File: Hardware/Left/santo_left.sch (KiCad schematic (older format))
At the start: 7 parts

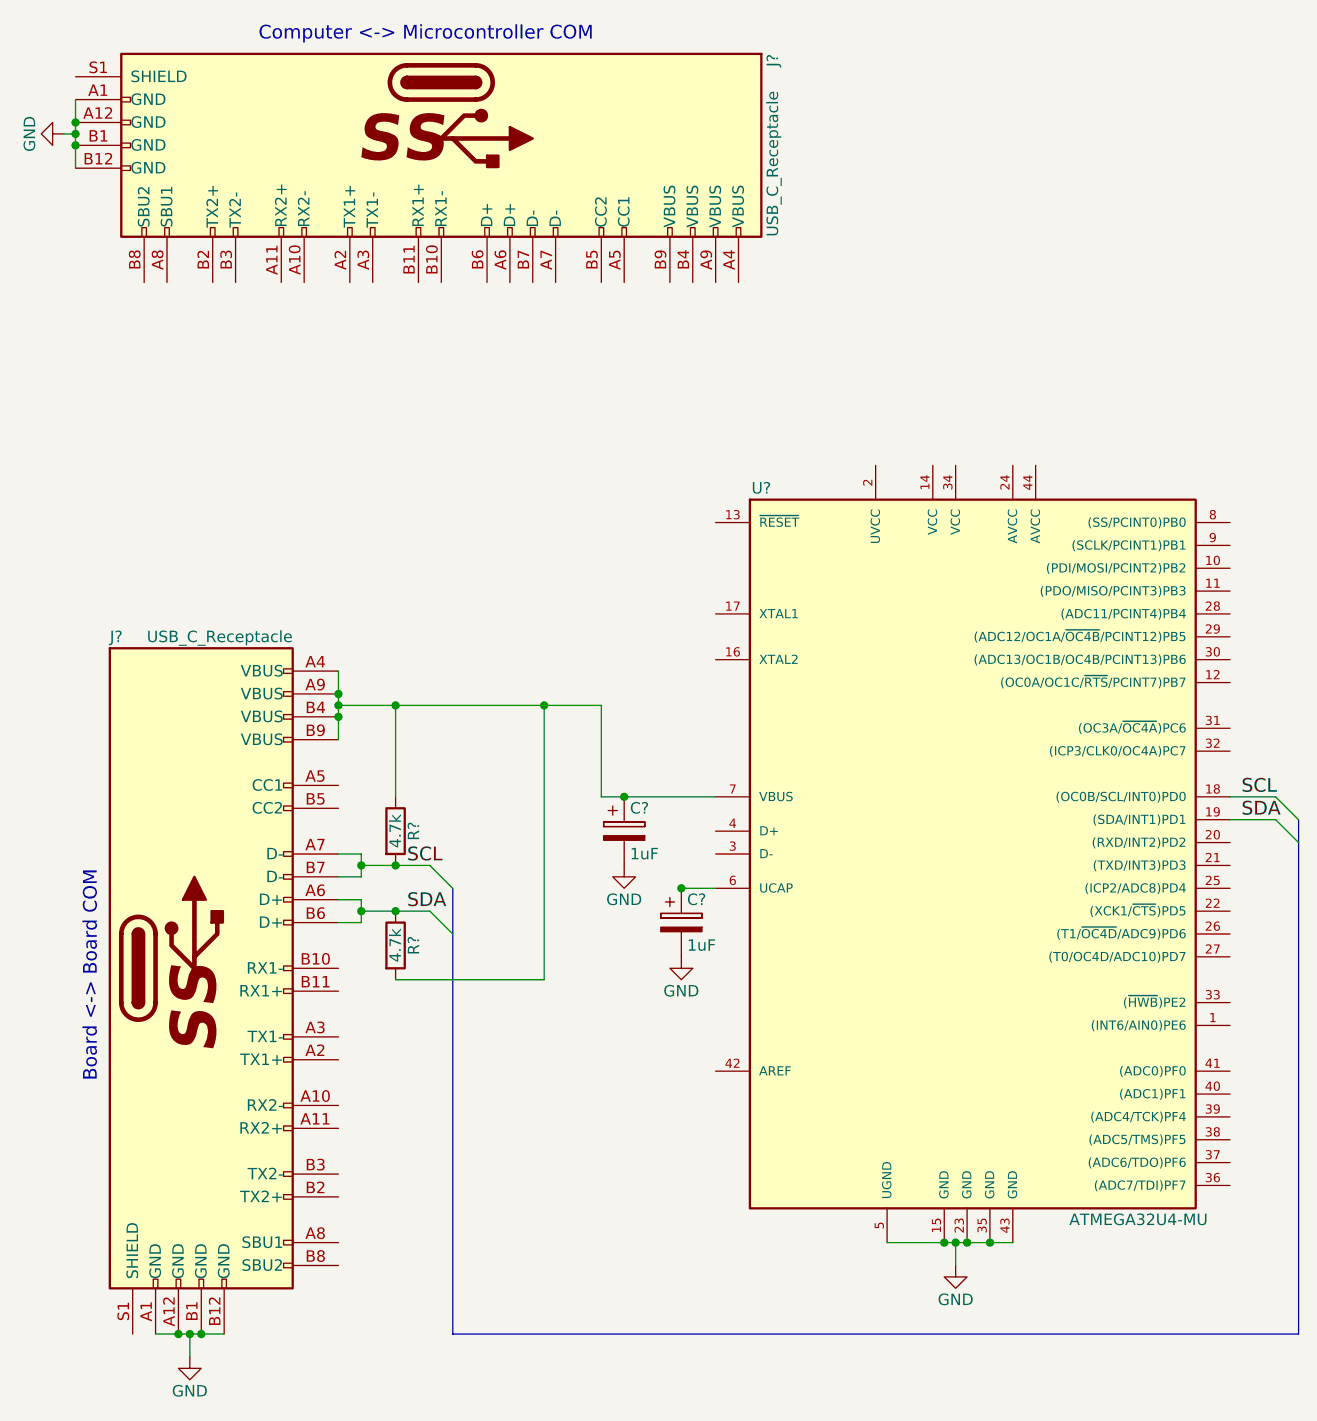
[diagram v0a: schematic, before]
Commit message: Wire up the PC <-> Board communication.
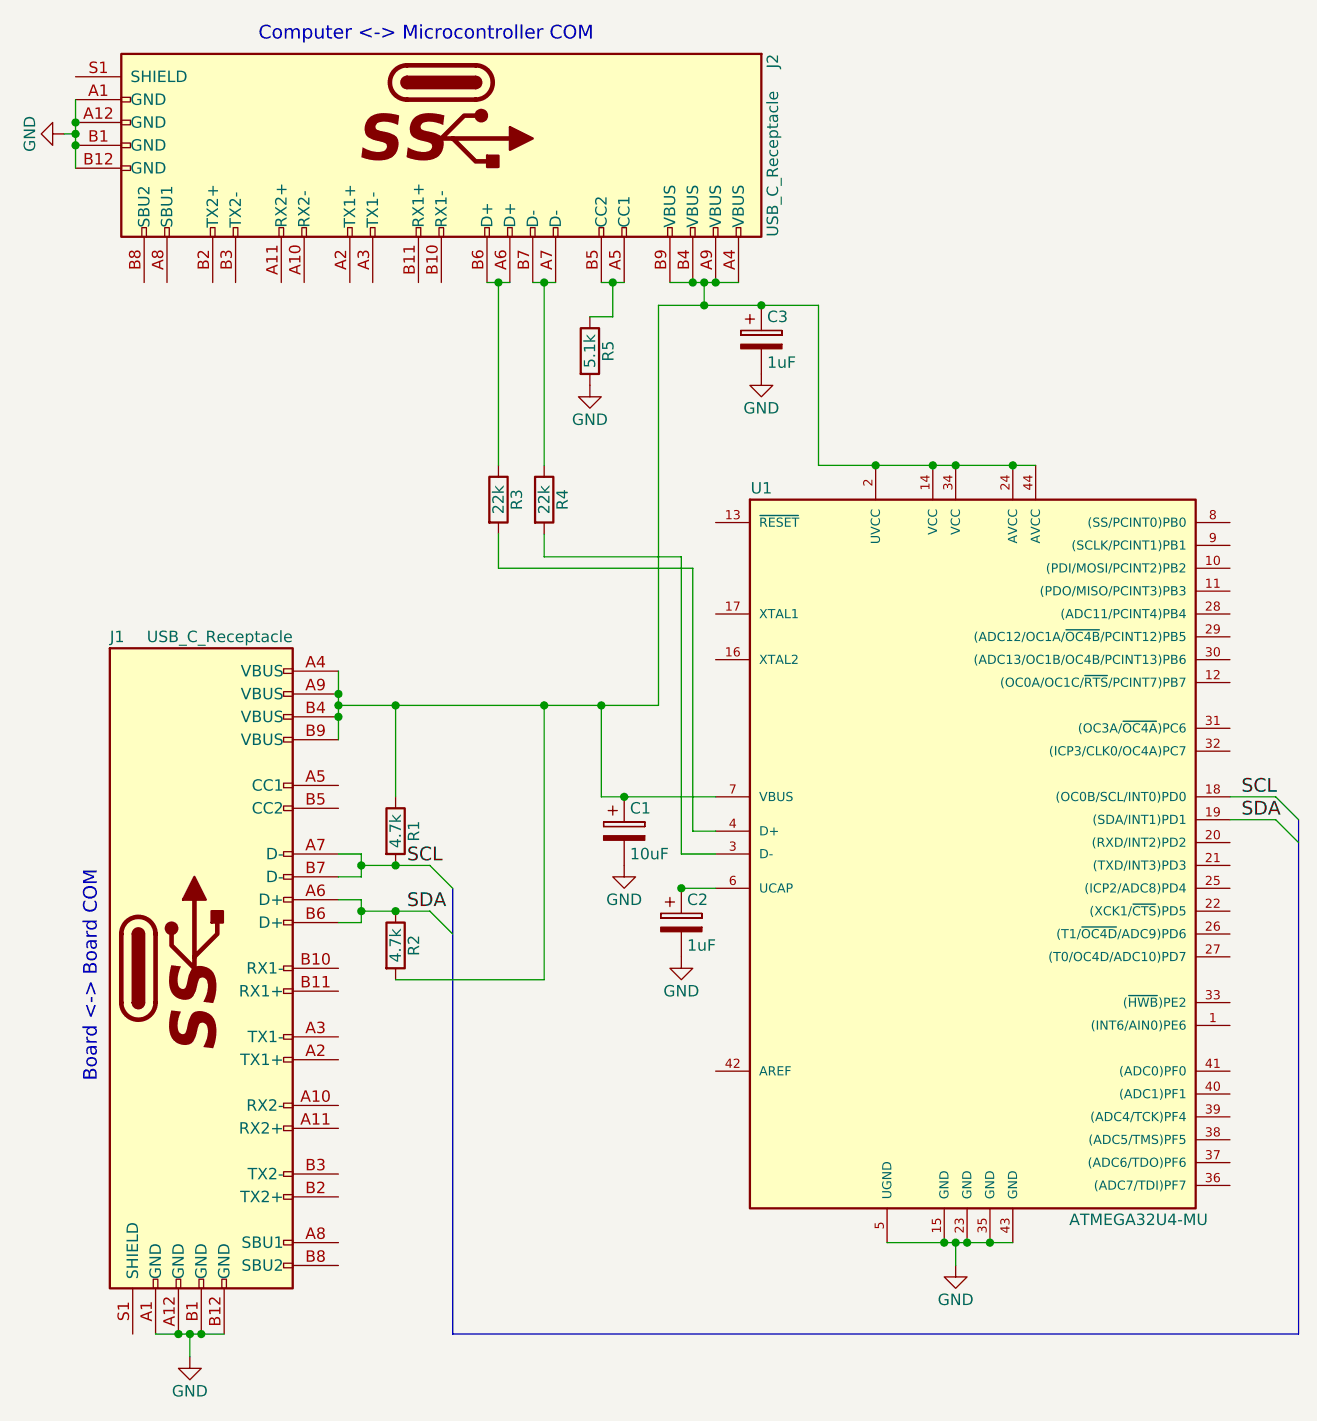
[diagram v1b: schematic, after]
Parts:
- added C3: 1uF, symbol CP
- added R3, R4: 22k, symbol R
- added R5: 5.1k, symbol R
- C1: renamed from C?; value 1uF -> 10uF
- gave numbers to parts that had none: 6
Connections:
- net GND: now also C3.2, R5.2
- net at U1.14 (VCC): now also C1.1, J1.A4 (VBUS), J1.A9 (VBUS), J1.B4 (VBUS), J1.B9 (VBUS), J2.A4 (VBUS), J2.A9 (VBUS), J2.B4 (VBUS), J2.B9 (VBUS), R1.1, R2.2, U1.2 (UVCC), U1.24 (AVCC), U1.34 (VCC), U1.44 (AVCC), U1.7 (VBUS), C3.1
- net at U1.3 (D-): now also R4.2
- net at U1.4 (D+): now also R3.2
- net at J2.A5 (CC1): now also J2.B5 (CC2), R5.1
- net at J2.A6 (D+): now also J2.B6 (D+), R3.1
- net at J2.A7 (D-): now also J2.B7 (D-), R4.1
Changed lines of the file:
@@
 $EndDescr
 $Comp
-L ATMEGA32U4-MU U?
+L ATMEGA32U4-MU U1
 U 1 1 5A091DA6
 P 4700 4300
-F 0 "U?" H 3750 6000 50  0000 C CNN
+F 0 "U1" H 3750 6000 50  0000 C CNN
 F 1 "ATMEGA32U4-MU" H 5400 2800 50  0000 C CNN
 F 2 "QFN44" H 4700 4300 50  0001 C CIN
@@
 $EndComp
 $Comp
-L USB_C_Receptacle J?
+L USB_C_Receptacle J2
 U 1 1 5A091DCC
 P 2350 1100
-F 0 "J?" H 1950 2550 50  0000 L CNN
+F 0 "J2" H 1950 2550 50  0000 L CNN
 F 1 "USB_C_Receptacle" H 2750 2550 50  0000 R CNN
 F 2 "" H 2500 1100 50  0001 C CNN
@@
 $EndComp
 $Comp
-L USB_C_Receptacle J?
+L USB_C_Receptacle J1
 U 1 1 5A091E31
 P 1300 4700
-F 0 "J?" H 900 6150 50  0000 L CNN
+F 0 "J1" H 900 6150 50  0000 L CNN
 F 1 "USB_C_Receptacle" H 1700 6150 50  0000 R CNN
 F 2 "" H 1450 4700 50  0001 C CNN
@@
 Entry Wire Line
 	6000 4050 6100 4150
-Wire Wire Line
-	5800 3950 6000 3950
-Wire Wire Line
-	5800 4050 6000 4050
-Wire Bus Line
-	6100 6300 6100 4050
-Wire Wire Line
-	1900 4200 2000 4200
-Wire Wire Line
-	2000 4300 1900 4300
-Wire Wire Line
-	1900 4400 2000 4400
-Wire Wire Line
-	1900 4500 2000 4500
-Wire Wire Line
-	2000 4200 2000 4300
-Wire Wire Line
-	2000 4500 2000 4400
-Connection ~ 2000 4250
-Connection ~ 2000 4450
-Wire Wire Line
-	3050 3950 3550 3950
-Wire Wire Line
-	1100 6300 1400 6300
-Wire Wire Line
-	1250 6300 1250 6400
-Connection ~ 1250 6300
-$Comp
-L GND #PWR?
+$Comp
+L GND #PWR2
 U 1 1 5A09277D
 P 1250 6400
-F 0 "#PWR?" H 1250 6150 50  0001 C CNN
+F 0 "#PWR2" H 1250 6150 50  0001 C CNN
 F 1 "GND" H 1250 6250 50  0000 C CNN
 F 2 "" H 1250 6400 50  0001 C CNN
@@
 	1    0    0    -1
 $EndComp
-Wire Wire Line
-	750  900  750  1200
-Wire Wire Line
-	750  1050 700  1050
-Connection ~ 750  1050
-$Comp
-L GND #PWR?
+$Comp
+L GND #PWR1
 U 1 1 5A0928F2
 P 700 1050
-F 0 "#PWR?" H 700 800 50  0001 C CNN
+F 0 "#PWR1" H 700 800 50  0001 C CNN
 F 1 "GND" H 700 900 50  0000 C CNN
 F 2 "" H 700 1050 50  0001 C CNN
@@
 	0    1    1    0
 $EndComp
-Wire Wire Line
-	3550 4350 3400 4350
-$Comp
-L CP C?
+$Comp
+L CP C2
 U 1 1 5A092A38
 P 3400 4500
-F 0 "C?" H 3425 4600 50  0000 L CNN
+F 0 "C2" H 3425 4600 50  0000 L CNN
 F 1 "1uF" H 3425 4400 50  0000 L CNN
 F 2 "" H 3438 4350 50  0001 C CNN
@@
 $EndComp
 $Comp
-L GND #PWR?
+L GND #PWR5
 U 1 1 5A092A79
 P 3400 4650
-F 0 "#PWR?" H 3400 4400 50  0001 C CNN
+F 0 "#PWR5" H 3400 4400 50  0001 C CNN
 F 1 "GND" H 3400 4500 50  0000 C CNN
 F 2 "" H 3400 4650 50  0001 C CNN
@@
 	1    0    0    -1
 $EndComp
+$Comp
+L CP C1
+U 1 1 5A0933EF
+P 3150 4100
+F 0 "C1" H 3175 4200 50  0000 L CNN
+F 1 "10uF" H 3175 4000 50  0000 L CNN
+F 2 "" H 3188 3950 50  0001 C CNN
+F 3 "" H 3150 4100 50  0001 C CNN
+	1    3150 4100
+	1    0    0    -1
+$EndComp
+$Comp
+L GND #PWR4
+U 1 1 5A09341E
+P 3150 4250
+F 0 "#PWR4" H 3150 4000 50  0001 C CNN
+F 1 "GND" H 3150 4100 50  0000 C CNN
+F 2 "" H 3150 4250 50  0001 C CNN
+F 3 "" H 3150 4250 50  0001 C CNN
+	1    3150 4250
+	1    0    0    -1
+$EndComp
+$Comp
+L GND #PWR7
+U 1 1 5A093698
+P 4600 6000
+F 0 "#PWR7" H 4600 5750 50  0001 C CNN
+F 1 "GND" H 4600 5850 50  0000 C CNN
+F 2 "" H 4600 6000 50  0001 C CNN
+F 3 "" H 4600 6000 50  0001 C CNN
+	1    4600 6000
+	1    0    0    -1
+$EndComp
+Text Label 5850 3950 0    60   ~ 0
+SCL
+Text Label 5850 4050 0    60   ~ 0
+SDA
+$Comp
+L R R1
+U 1 1 5A093ADE
+P 2150 4100
+F 0 "R1" V 2230 4100 50  0000 C CNN
+F 1 "4.7k" V 2150 4100 50  0000 C CNN
+F 2 "" V 2080 4100 50  0001 C CNN
+F 3 "" H 2150 4100 50  0001 C CNN
+	1    2150 4100
+	1    0    0    -1
+$EndComp
+$Comp
+L R R2
+U 1 1 5A093B19
+P 2150 4600
+F 0 "R2" V 2230 4600 50  0000 C CNN
+F 1 "4.7k" V 2150 4600 50  0000 C CNN
+F 2 "" V 2080 4600 50  0001 C CNN
+F 3 "" H 2150 4600 50  0001 C CNN
+	1    2150 4600
+	1    0    0    -1
+$EndComp
+Entry Wire Line
+	2300 4250 2400 4350
+Entry Wire Line
+	2300 4450 2400 4550
+Text Label 2200 4250 0    60   ~ 0
+SCL
+Text Label 2200 4450 0    60   ~ 0
+SDA
+$Comp
+L CP C3
+U 1 1 5A094C59
+P 3750 1950
+F 0 "C3" H 3775 2050 50  0000 L CNN
+F 1 "1uF" H 3775 1850 50  0000 L CNN
+F 2 "" H 3788 1800 50  0001 C CNN
+F 3 "" H 3750 1950 50  0001 C CNN
+	1    3750 1950
+	1    0    0    -1
+$EndComp
+$Comp
+L GND #PWR6
+U 1 1 5A094E64
+P 3750 2100
+F 0 "#PWR6" H 3750 1850 50  0001 C CNN
+F 1 "GND" H 3750 1950 50  0000 C CNN
+F 2 "" H 3750 2100 50  0001 C CNN
+F 3 "" H 3750 2100 50  0001 C CNN
+	1    3750 2100
+	1    0    0    -1
+$EndComp
+$Comp
+L R R5
+U 1 1 5A095F9F
+P 3000 2000
+F 0 "R5" V 3080 2000 50  0000 C CNN
+F 1 "5.1k" V 3000 2000 50  0000 C CNN
+F 2 "" V 2930 2000 50  0001 C CNN
+F 3 "" H 3000 2000 50  0001 C CNN
+	1    3000 2000
+	1    0    0    -1
+$EndComp
+$Comp
+L GND #PWR3
+U 1 1 5A095FF2
+P 3000 2150
+F 0 "#PWR3" H 3000 1900 50  0001 C CNN
+F 1 "GND" H 3000 2000 50  0000 C CNN
+F 2 "" H 3000 2150 50  0001 C CNN
+F 3 "" H 3000 2150 50  0001 C CNN
+	1    3000 2150
+	1    0    0    -1
+$EndComp
+Wire Wire Line
+	5800 3950 6000 3950
+Wire Wire Line
+	5800 4050 6000 4050
+Wire Bus Line
+	6100 6300 6100 4050
+Wire Wire Line
+	1900 4200 2000 4200
+Wire Wire Line
+	2000 4300 1900 4300
+Wire Wire Line
+	1900 4400 2000 4400
+Wire Wire Line
+	1900 4500 2000 4500
+Wire Wire Line
+	2000 4200 2000 4300
+Wire Wire Line
+	2000 4500 2000 4400
+Connection ~ 2000 4250
+Connection ~ 2000 4450
+Wire Wire Line
+	3050 3950 3550 3950
+Wire Wire Line
+	1100 6300 1400 6300
+Wire Wire Line
+	1250 6300 1250 6400
+Connection ~ 1250 6300
+Wire Wire Line
+	750  900  750  1200
+Wire Wire Line
+	750  1050 700  1050
+Connection ~ 750  1050
+Wire Wire Line
+	3550 4350 3400 4350
 Wire Wire Line
 	3050 3950 3050 3550
 Wire Wire Line
-	3050 3550 1900 3550
+	1900 3550 3300 3550
 Wire Wire Line
 	1900 3400 1900 3700
@@
 Connection ~ 750  1000
 Connection ~ 750  1100
-$Comp
-L CP C?
-U 1 1 5A0933EF
-P 3150 4100
-F 0 "C?" H 3175 4200 50  0000 L CNN
-F 1 "1uF" H 3175 4000 50  0000 L CNN
-F 2 "" H 3188 3950 50  0001 C CNN
-F 3 "" H 3150 4100 50  0001 C CNN
-	1    3150 4100
-	1    0    0    -1
-$EndComp
-$Comp
-L GND #PWR?
-U 1 1 5A09341E
-P 3150 4250
-F 0 "#PWR?" H 3150 4000 50  0001 C CNN
-F 1 "GND" H 3150 4100 50  0000 C CNN
-F 2 "" H 3150 4250 50  0001 C CNN
-F 3 "" H 3150 4250 50  0001 C CNN
-	1    3150 4250
-	1    0    0    -1
-$EndComp
 Connection ~ 3150 3950
 Connection ~ 3400 4350
@@
 	4600 5900 4600 6000
 Connection ~ 4600 5900
-$Comp
-L GND #PWR?
-U 1 1 5A093698
-P 4600 6000
-F 0 "#PWR?" H 4600 5750 50  0001 C CNN
-F 1 "GND" H 4600 5850 50  0000 C CNN
-F 2 "" H 4600 6000 50  0001 C CNN
-F 3 "" H 4600 6000 50  0001 C CNN
-	1    4600 6000
-	1    0    0    -1
-$EndComp
-Text Label 5850 3950 0    60   ~ 0
-SCL
-Text Label 5850 4050 0    60   ~ 0
-SDA
 Wire Wire Line
 	2000 4250 2300 4250
 Wire Wire Line
 	2000 4450 2300 4450
-$Comp
-L R R?
-U 1 1 5A093ADE
-P 2150 4100
-F 0 "R?" V 2230 4100 50  0000 C CNN
-F 1 "4.7k" V 2150 4100 50  0000 C CNN
-F 2 "" V 2080 4100 50  0001 C CNN
-F 3 "" H 2150 4100 50  0001 C CNN
-	1    2150 4100
-	1    0    0    -1
-$EndComp
-$Comp
-L R R?
-U 1 1 5A093B19
-P 2150 4600
-F 0 "R?" V 2230 4600 50  0000 C CNN
-F 1 "4.7k" V 2150 4600 50  0000 C CNN
-F 2 "" V 2080 4600 50  0001 C CNN
-F 3 "" H 2150 4600 50  0001 C CNN
-	1    2150 4600
-	1    0    0    -1
-$EndComp
 Wire Wire Line
 	2150 3950 2150 3550
@@
 Connection ~ 2150 4250
 Connection ~ 2150 4450
-Entry Wire Line
-	2300 4250 2400 4350
-Entry Wire Line
-	2300 4450 2400 4550
 Wire Bus Line
 	2400 4350 2400 6300
 Wire Bus Line
 	2400 6300 6100 6300
-Text Label 2200 4250 0    60   ~ 0
-SCL
-Text Label 2200 4450 0    60   ~ 0
-SDA
+Wire Wire Line
+	3350 1700 3650 1700
+Connection ~ 3550 1700
+Connection ~ 3450 1700
+Wire Wire Line
+	3500 1700 3500 1800
+Connection ~ 3500 1700
+Wire Wire Line
+	3300 3550 3300 1800
+Connection ~ 3500 1800
+Connection ~ 3050 3550
+Wire Wire Line
+	4000 1800 4000 2500
+Wire Wire Line
+	4000 2500 4950 2500
+Wire Wire Line
+	3300 1800 4000 1800
+Connection ~ 3750 1800
+Connection ~ 4250 2500
+Connection ~ 4500 2500
+Connection ~ 4600 2500
+Connection ~ 4850 2500
+Wire Wire Line
+	3150 1700 3050 1700
+Wire Wire Line
+	3100 1700 3100 1850
+Wire Wire Line
+	3100 1850 3000 1850
+Connection ~ 3100 1700
+Wire Wire Line
+	2550 1700 2650 1700
+Wire Wire Line
+	2750 1700 2850 1700
+Wire Wire Line
+	2600 1700 2600 2500
+Connection ~ 2600 1700
+Wire Wire Line
+	2800 1700 2800 2500
+Connection ~ 2800 1700
+$Comp
+L R R3
+U 1 1 5A096599
+P 2600 2650
+F 0 "R3" V 2680 2650 50  0000 C CNN
+F 1 "22k" V 2600 2650 50  0000 C CNN
+F 2 "" V 2530 2650 50  0001 C CNN
+F 3 "" H 2600 2650 50  0001 C CNN
+	1    2600 2650
+	1    0    0    -1
+$EndComp
+$Comp
+L R R4
+U 1 1 5A0965D0
+P 2800 2650
+F 0 "R4" V 2880 2650 50  0000 C CNN
+F 1 "22k" V 2800 2650 50  0000 C CNN
+F 2 "" V 2730 2650 50  0001 C CNN
+F 3 "" H 2800 2650 50  0001 C CNN
+	1    2800 2650
+	1    0    0    -1
+$EndComp
+Wire Wire Line
+	3550 4100 3450 4100
+Wire Wire Line
+	3450 4100 3450 2950
+Wire Wire Line
+	3450 2950 2600 2950
+Wire Wire Line
+	2600 2950 2600 2800
+Wire Wire Line
+	3550 4200 3400 4200
+Wire Wire Line
+	3400 4200 3400 2900
+Wire Wire Line
+	3400 2900 2800 2900
+Wire Wire Line
+	2800 2900 2800 2800
 $EndSCHEMATC
